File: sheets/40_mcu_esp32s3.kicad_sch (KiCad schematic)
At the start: 20 parts, among them J401 USB4105-GF-A, J402 UART0, SW401 RESET, SW402 BOOT, U401 ESP32-S3-WROOM-1-N8R2, U402 USBLC6-2SC6

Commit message: [Codex] Integra cierre de Claude y valida sincronizacion previa al layout
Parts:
- removed D401: PMEG3020EH, Diode_SMD:D_SOD-123F, symbol Device:D_Schottky
- removed JP401: BANCO_USB, Jumper:SolderJumper-2_P1.3mm_Open_RoundedPad1.0x1.5mm, symbol Jumper:SolderJumper_2_Open
- R401: Notes Pull-up de EN (RC de Espressif: 10k + 1 uF). También es el pull-up del WDO (drenador abierto) del TPS3431 en 80_supervision. -> Pull-up de EN (RC de Espressif: 10k + 1 uF). También es el pull-up del WDO (drenador abierto) del TPS3828 en 80_supervision.
- U401: Notes 8 MB flash quad + 2 MB PSRAM quad, antena PCB, -40 a +85 C (las variantes R8/R16 con PSRAM octal llegan solo a 65 C). PSRAM quad: IO35-IO37 libres (WROOM-1 v1.8, tabla 3-1, nota b). LCSC C2913204. Pad 41 (EPAD) y pines 1/40 a GND_VEH. Antena al borde de la placa con keepout (ver nota de layout). -> 8 MB flash quad + 2 MB PSRAM quad, antena PCB, -40 a +85 C (las variantes R8/R16 con PSRAM octal llegan solo a 65 C). PSRAM quad: IO35-IO37 libres (WROOM-1 v1.8, tabla 3-1, nota b). LCSC C2913204. Pad 41 (EPAD) y pines 1/40 a GND_VEH. Antena al borde de la placa con keepout (ver nota de layout). IMPORTANTE: IO35-IO37 se usan como GPIO (DO1_EN, DO2_EN, DO1_DIAG); solo es valido con PSRAM quad (N8R2) o sin PSRAM. NO reemplazar por variantes con PSRAM octal (R8).
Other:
- note added: "ASIGNACIÓN DE PINES (aprobada 2026-10-27; fuentes: WROOM-1 v1.8 tabla 3-1, ESP32-S3 Series v2.2 tablas 2-1 y 2-2) Criterios: VMON solo en ADC1 (ADC2 no se puede usar con WiFi). GPIO1–14, 17, 18: glitch BAJO de ~60 µs al encender → solo CS, SCK, MOSI, LEDs, entradas resistivas o analógicas, WDI. Señales críticas en pines sin glitch ni pull: IO21, IO35–38, IO40–42, IO47/48. SPI en los pines IO MUX 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"
- note added: "EN: RC de Espressif + WDO del TPS3828 + RESET"
- note removed: "ASIGNACIÓN DE PINES (aprobada 2026-10-27; fuentes: WROOM-1 v1.8 tabla 3-1, ESP32-S3 Series v2.2 tablas 2-1 y 2-2) Criterios: VMON solo en ADC1 (ADC2 no se puede usar con WiFi). GPIO1–14, 17, 18: glitch BAJO de ~60 µs al encender → solo CS, SCK, MOSI, LEDs, entradas resistivas o analógicas, WDI/WD_EN. Señales críticas en pines sin glitch ni pull: IO21, IO35–38, IO40–42, IO47/48. SPI en los pines I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"
- note removed: "EN: RC de Espressif + WDO del TPS3431 + RESET"
- note removed: "OPCIÓN DE BANCO (DNP): +5V_VEH ← JP401 ← D401 ← VBUS +5V_VEH ≈ 4.6 V; CAN no garantizado en este modo."

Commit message: update pcb layout
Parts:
- removed SW401: RESET, Button_Switch_THT:SW_PUSH_6mm, symbol Switch:SW_Push
- removed SW402: BOOT, Button_Switch_THT:SW_PUSH_6mm, symbol Switch:SW_Push
- added SW401: RESET, easyeda2kicad:SW-SMD_L3.9-W3.0-P4.45, symbol easyeda2kicad:TS-1088-AR02016
- added SW402: BOOT, easyeda2kicad:SW-SMD_L3.9-W3.0-P4.45, symbol easyeda2kicad:TS-1088-AR02016
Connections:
- net BOOT: now also SW402.2
- net GND_VEH: now also SW401.1, SW402.1
- net MCU_RST_N: now also SW401.2
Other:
- moved on the sheet: C403, TP401

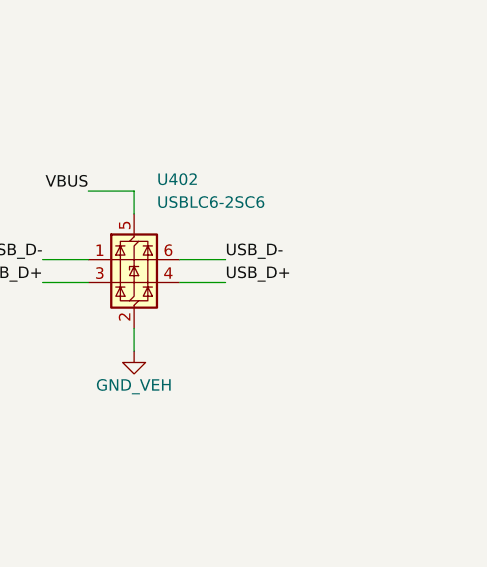
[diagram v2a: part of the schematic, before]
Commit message: [Codex] ruteo etapa 3: agrega C404 y completa avance salvo escape USB
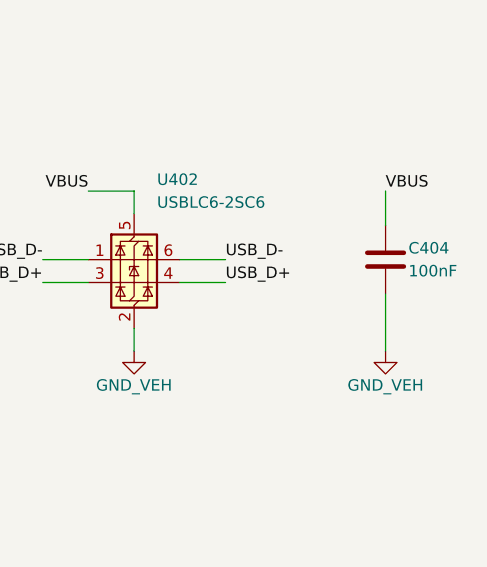
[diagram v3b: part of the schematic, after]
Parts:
- added C404: 100nF, Capacitor_SMD:C_0603_1608Metric, symbol Device:C
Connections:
- net GND_VEH: now also C404.2
- net VBUS: now also C404.1
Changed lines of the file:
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@@
 		)
 	)
+	(symbol
+		(lib_id "Device:C")
+		(at 365.7600 63.5000 0)
+		(unit 1)
+		(body_style 1)
+		(exclude_from_sim no)
+		(in_bom yes)
+		(on_board yes)
+		(in_pos_files yes)
+		(dnp no)
+		(property "Reference" "C404"
+			(at 368.3000 62.2300 0)
+			(show_name no)
+			(do_not_autoplace no)
+			(effects
+				(font
+					(size 1.27 1.27)
+				)
+				(justify left)
+			)
+		)
+		(property "Value" "100nF"
+			(at 368.3000 64.7700 0)
+			(show_name no)
+			(do_not_autoplace no)
+			(effects
+				(font
+					(size 1.27 1.27)
+				)
+				(justify left)
+			)
+		)
+		(property "Footprint" "Capacitor_SMD:C_0603_1608Metric"
+			(at 365.7600 63.5000 0)
+			(hide yes)
+			(show_name no)
+			(do_not_autoplace no)
+			(effects
+				(font
+					(size 1.27 1.27)
+				)
+			)
+		)
+		(property "Datasheet" "https://www.murata.com/en-global/products/productdetail?partno=GCM188R71H104KA57D"
+			(at 365.7600 63.5000 0)
+			(hide yes)
+			(show_name no)
+			(do_not_autoplace no)
+			(effects
+				(font
+					(size 1.27 1.27)
+				)
+			)
+		)
+		(property "Description" ""
+			(at 365.7600 63.5000 0)
+			(hide yes)
+			(show_name no)
+			(do_not_autoplace no)
+			(effects
+				(font
+					(size 1.27 1.27)
+				)
+			)
+		)
+		(property "MPN" "GCM188R71H104KA57D"
+			(at 365.7600 63.5000 0)
+			(hide yes)
+			(show_name no)
+			(do_not_autoplace no)
+			(effects
+				(font
+					(size 1.27 1.27)
+				)
+			)
+		)
+		(property "Manufacturer" "Murata"
+			(at 365.7600 63.5000 0)
+			(hide yes)
+			(show_name no)
+			(do_not_autoplace no)
+			(effects
+				(font
+					(size 1.27 1.27)
+				)
+			)
+		)
+		(property "Notes" "Desacople VBUS del USBLC6-2SC6: 100 nF, X7R, 50 V, 0603; no alimenta el riel +5V. Agregado despues de placement-v1, autorizado en etapa 3."
+			(at 365.7600 63.5000 0)
+			(hide yes)
+			(show_name no)
+			(do_not_autoplace no)
+			(effects
+				(font
+					(size 1.27 1.27)
+				)
+			)
+		)
+		(property "DNP" ""
+			(at 365.7600 63.5000 0)
+			(hide yes)
+			(show_name no)
+			(do_not_autoplace no)
+			(effects
+				(font
+					(size 1.27 1.27)
+				)
+			)
+		)
+		(pin "1"
+		)
+		(pin "2"
+		)
+		(instances
+			(project "INCLI-VA"
+				(path "/7fd92c2b-4254-4d73-93ba-bfde861bede3/712b3cf0-3806-4b78-89c5-204f7bed5fb6"
+					(reference "C404")
+					(unit 1)
+				)
+			)
+		)
+	)
+	(symbol
+		(lib_id "INCLI-VA:GND_VEH")
+		(at 365.7600 73.6600 0)
+		(unit 1)
+		(body_style 1)
+		(exclude_from_sim no)
+		(in_bom no)
+		(on_board yes)
+		(in_pos_files no)
+		(dnp no)
+		(property "Reference" "#PWR416"
+			(at 365.7600 80.0100 0)
+			(hide yes)
+			(show_name no)
+			(do_not_autoplace no)
+			(effects
+				(font
+					(size 1.27 1.27)
+				)
+			)
+		)
+		(property "Value" "GND_VEH"
+			(at 365.7600 77.4700 0)
+			(show_name no)
+			(do_not_autoplace no)
+			(effects
+				(font
+					(size 1.27 1.27)
+				)
+			)
+		)
+		(property "Footprint" ""
+			(at 365.7600 73.6600 0)
+			(hide yes)
+			(show_name no)
+			(do_not_autoplace no)
+			(effects
+				(font
+					(size 1.27 1.27)
+				)
+			)
+		)
+		(property "Datasheet" ""
+			(at 365.7600 73.6600 0)
+			(hide yes)
+			(show_name no)
+			(do_not_autoplace no)
+			(effects
+				(font
+					(size 1.27 1.27)
+				)
+			)
+		)
+		(property "Description" ""
+			(at 365.7600 73.6600 0)
+			(hide yes)
+			(show_name no)
+			(do_not_autoplace no)
+			(effects
+				(font
+					(size 1.27 1.27)
+				)
+			)
+		)
+		(pin "1"
+		)
+		(instances
+			(project "INCLI-VA"
+				(path "/7fd92c2b-4254-4d73-93ba-bfde861bede3/712b3cf0-3806-4b78-89c5-204f7bed5fb6"
+					(reference "#PWR416")
+					(unit 1)
+				)
+			)
+		)
+	)
+	(wire (pts (xy 365.76 55.88) (xy 365.76 59.69)) (stroke (width 0) (type default)))
+	(wire (pts (xy 365.76 67.31) (xy 365.76 73.66)) (stroke (width 0) (type default)))
+	(label "VBUS" (at 365.76 55.88 0) (effects (font (size 1.27 1.27)) (justify left bottom)))
 )
